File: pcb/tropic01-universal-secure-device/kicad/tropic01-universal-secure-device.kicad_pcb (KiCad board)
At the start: 4 copper layers, 44 x 36 mm, 84 parts, among them J1 USB4105-GF-A, J2 ER-TFT024IPS-3 50P FFC, J6 SM04B-SRSS-TB, J9 S2B-PH-SM4-TB, SW1 EVQP7J01P, U1 STM32U585VIT6, U10 BQ24074RGTR, U11 OPTIGA-TRUST-M-SLS32AIA, U13 TPS22917DBVR, U14 TPS22917DBVR, U15 TPS61165DBVR, U2 TR01-C2P-T301, U3 TPS62840DLCR, U4 TPS22917DBVR, U5 W25Q128JVSIQ, U7 TPD4E05U06DQAR, U8 TPS2553DBVR, U9 ST25R3916B-AQET, X1 16MHz, X3 FA-238 27.12MHz

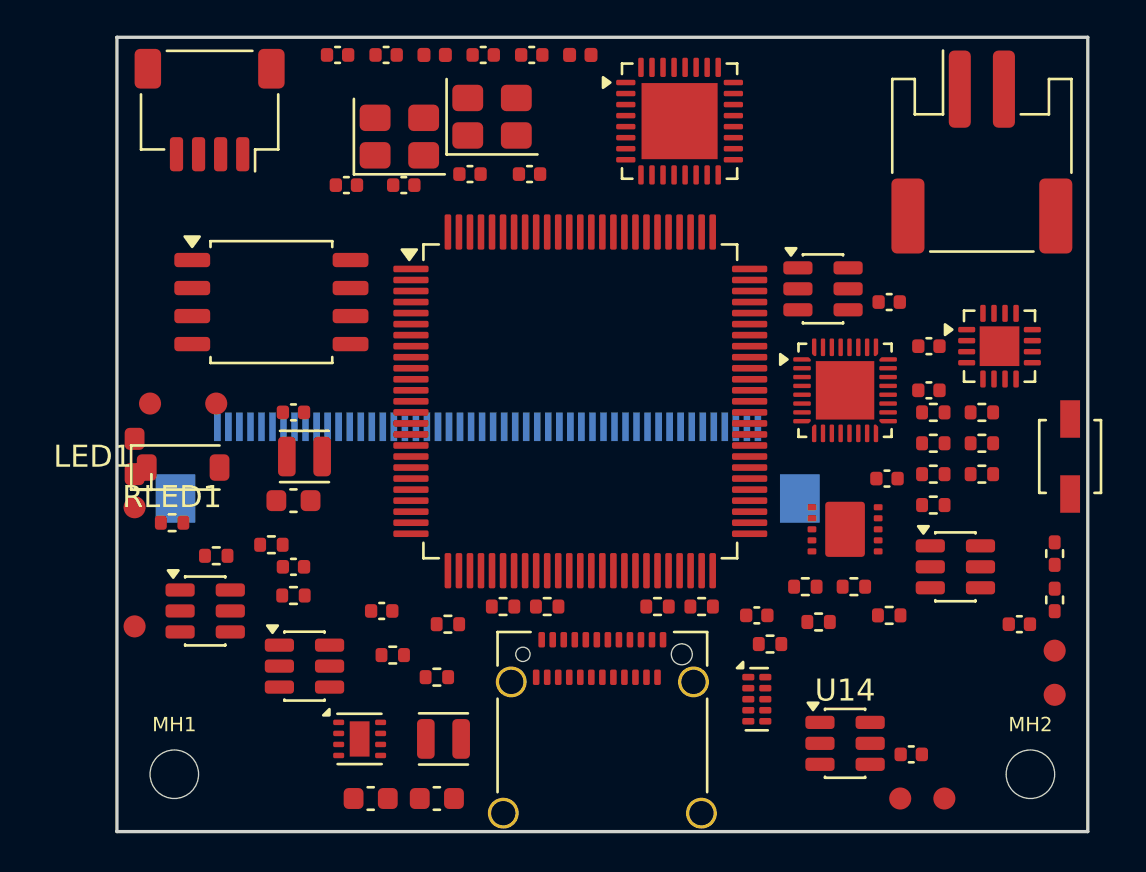
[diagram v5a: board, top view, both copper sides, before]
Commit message: hardware: resolve all real placement collisions; DRC 23 -> 2
Collision-aware re-placement (pcbnew, tested against every other footprint
courtyard) moves the misplaced backlight Schottky D15 and the crystal load caps
C18/C19 into free space, clearing all courtyard overlaps, the LED1/D15 short,
and the solder-mask bridge. Hiding the LED1/RLED1/MH1/MH2 reference fields
clears the remaining silk violations.

The only 2 remaining DRC items are the USB-C J1 shield pads at the board edge,
which is intentional for an edge-mounted receptacle (it must protrude through
the case opening). They should be marked Excluded in the KiCad DRC dialog
before the final fab package. Note: C19 landed ~8 mm from X1 — fine for DRC but
a crystal-load-cap proximity refinement for the routing pass.
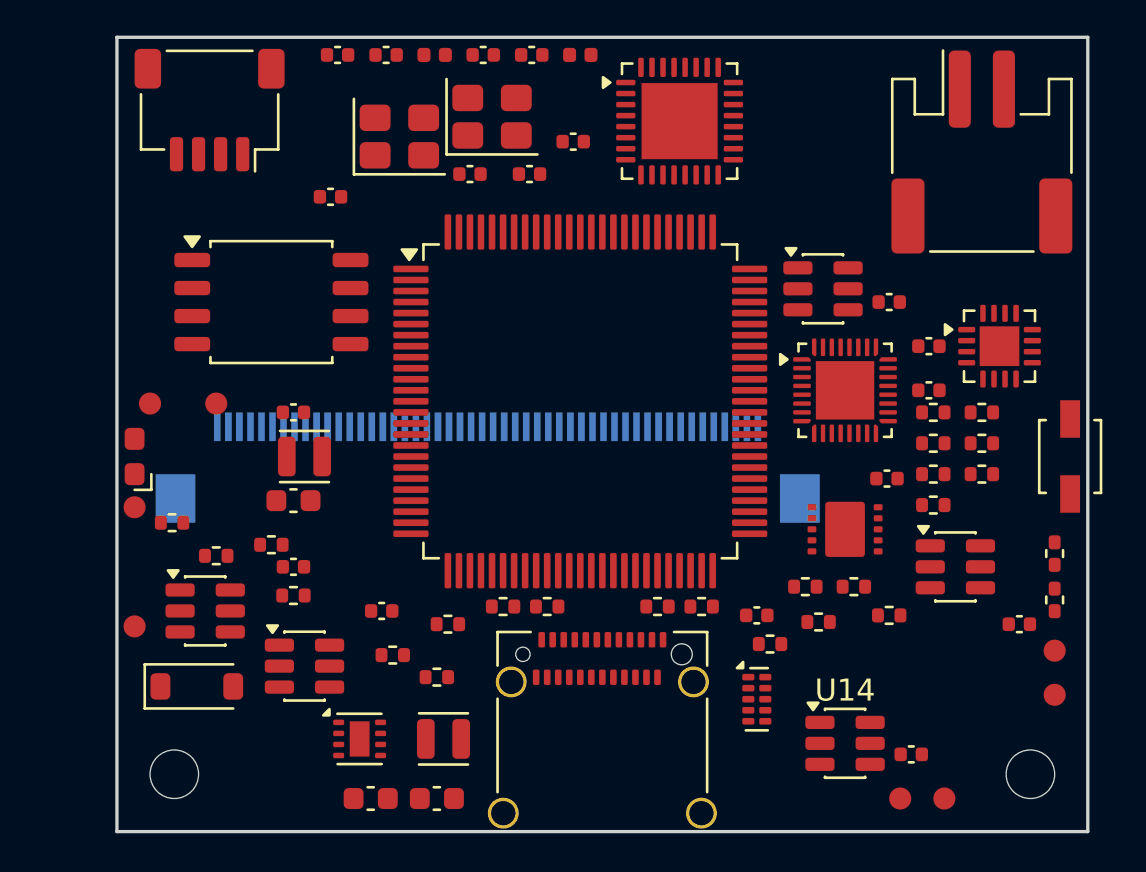
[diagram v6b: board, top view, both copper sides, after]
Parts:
- moved D15 9.94 mm to (13.6, 63.4)
- moved C19 7.93 mm to (30.7, 38.7)
- moved C18 0.89 mm to (19.7, 41.2)
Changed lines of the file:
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@@
 			(at 0 -1.9 0)
 			(layer "F.SilkS")
+			(hide yes)
 			(effects
 				(font
@@
 			(at 0 -2.25 0)
 			(layer "F.SilkS")
+			(hide yes)
 			(effects
 				(font
@@
 			(at 0 -2.25 0)
 			(layer "F.SilkS")
+			(hide yes)
 			(effects
 				(font
@@
 	(footprint "Diode_SMD:D_SOD-123"
 		(layer "F.Cu")
-		(at 13 53.5)
+		(at 13.62 63.419999)
 		(descr "SOD-123")
 		(tags "SOD-123")
@@
 			(at 0 -1.17 0)
 			(layer "F.SilkS")
+			(hide yes)
 			(effects
 				(font
@@
 	(footprint "Capacitor_SMD:C_0402_1005Metric"
 		(layer "F.Cu")
-		(at 20.4 40.7)
+		(at 19.68 41.229999)
 		(descr "Capacitor SMD 0402 (1005 Metric), square (rectangular) end terminal, IPC-7351 nominal, (Body size source: IPC-SM-782 page 76, https://www.pcb-3d.com/wordpress/wp-content/uploads/ipc-sm-782a_amendment_1_and_2.pdf)")
 		(tags "capacitor")
@@
 	(footprint "Capacitor_SMD:C_0402_1005Metric"
 		(layer "F.Cu")
-		(at 23 40.7)
+		(at 30.68 38.729999)
 		(descr "Capacitor SMD 0402 (1005 Metric), square (rectangular) end terminal, IPC-7351 nominal, (Body size source: IPC-SM-782 page 76, https://www.pcb-3d.com/wordpress/wp-content/uploads/ipc-sm-782a_amendment_1_and_2.pdf)")
 		(tags "capacitor")

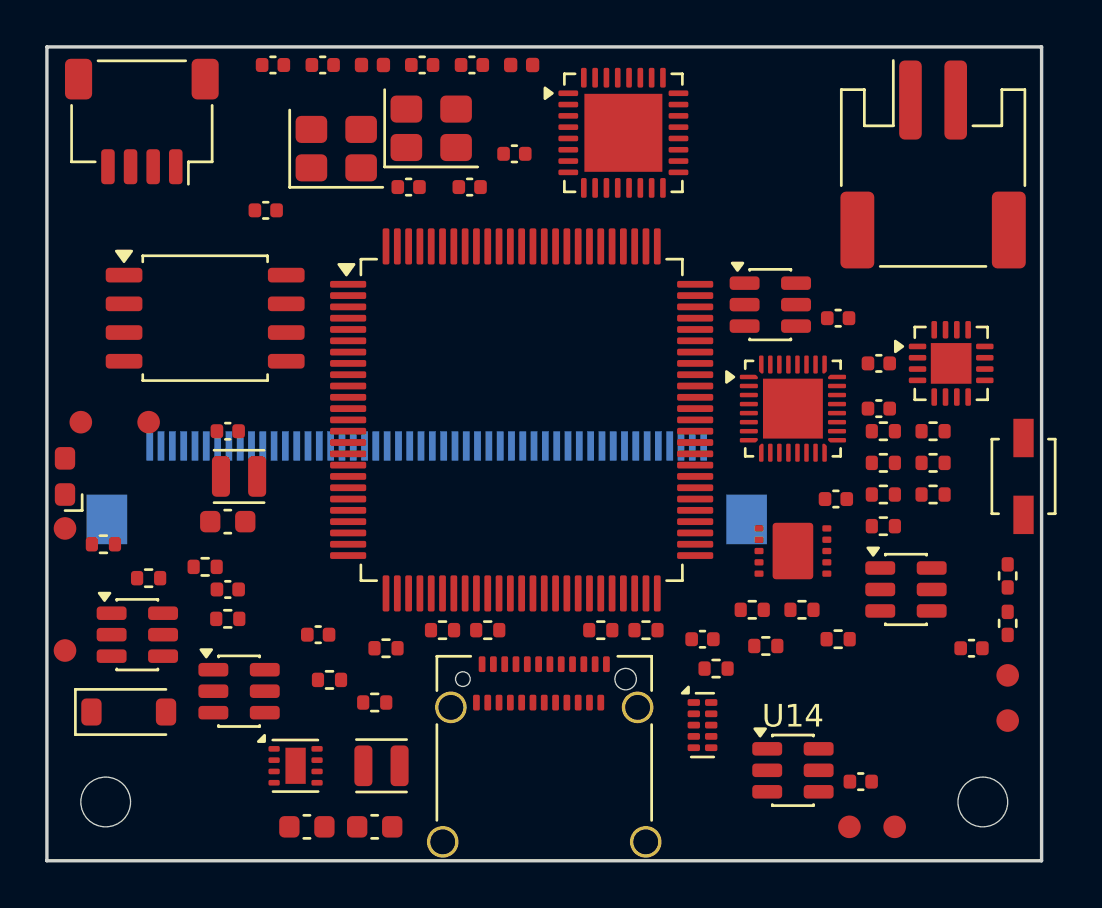
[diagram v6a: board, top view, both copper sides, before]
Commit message: hardware: connectivity-aware passive re-placement (improves routability)
Re-place every passive next to the component it shares the most signal nets with
(crystal load caps to X1, decoupling to its IC, pull-ups to their bus), keeping
the mechanical anchors fixed (USB-C, display FFC, button, mounting holes, ICs),
with full courtyard-collision avoidance and 0.6 mm edge margin.

Effect: Freerouting drops from 70 to 46 unrouted nets on the same netlist -
better placement directly improves routability, as expected. DRC stays clean
(2 intentional USB-C edge items + 2 minor silk). The user's original manual
passive placement was the main routing limiter.
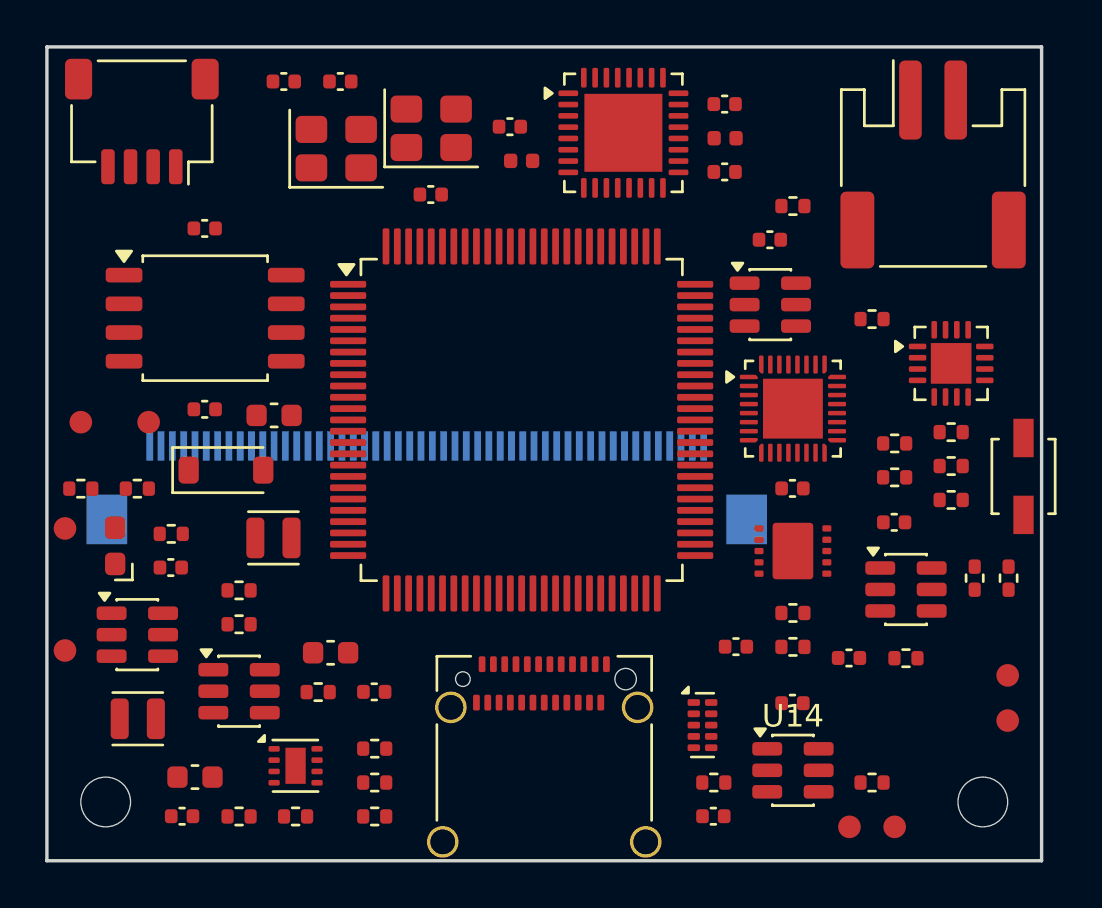
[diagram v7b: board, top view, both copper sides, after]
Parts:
- moved R23 23.3 mm to (18.5, 59.5)
- moved C2 18.7 mm to (20.0, 50.3)
- moved C31 16.1 mm to (17.0, 50.0)
- moved R19 15.2 mm to (11.5, 53.5)
- moved R17 14.7 mm to (43.0, 41.0)
- moved C32 13.5 mm to (40.0, 36.5)
- moved C4 13.1 mm to (45.5, 61.0)
- moved R4 13.1 mm to (24.5, 65.0)
- moved C3 12.3 mm to (40.5, 60.5)
- moved C33 12.1 mm to (40.0, 39.5)
- moved R2 12.1 mm to (39.5, 66.5)
- moved R3 12.1 mm to (24.5, 66.5)
- moved L15 11.6 mm to (14.0, 63.7)
- moved D15 11.5 mm to (17.9, 52.7)
- moved C15 11.4 mm to (16.5, 66.3)
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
